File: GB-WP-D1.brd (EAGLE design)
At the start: 39.7 x 44.1 mm, 9 parts

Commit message: Add files via upload
WEMOS D1 mini size
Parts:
- removed JP2: (no value), pinhead_v2:1X05/OCT
- removed JP5: (no value), pinhead_v2:1X04/OCT
- added U$3: KAMENRIDER_LOGOV2_COLOR_OPAC, kamenrider:10_6_V2
- moved JP4 7.61 mm to (12.6, 27.7)
- moved U$2 7.61 mm to (12.6, 33.8)
- moved LED1 6.52 mm to (22.0, 32.5)
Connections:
- net 3.3V: no longer JP2.5, JP5.3
- net 5V: no longer JP2.4
- net D0: no longer JP2.1
- net D2: no longer JP5.1
- net D3: no longer JP2.2
- net GND: no longer JP2.3, JP5.4
- net N$7: no longer JP5.2
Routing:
- net 3.3V: track 114.3 -> 53.0 mm
- net D3: track 52.7 -> 0.00 mm, vias 1 -> 0
- net GND: track 90.4 -> 44.6 mm, vias 3 -> 1
- net 5V: track 43.4 -> 0.00 mm, vias 1 -> 0
- net D0: track 24.4 -> 0.00 mm
- net N$7: track 46.6 -> 25.7 mm
- net D2: track 41.0 -> 23.9 mm
- net D7: track 35.1 -> 27.5 mm
- net D6: track 35.1 -> 27.5 mm
- net D5: track 32.2 -> 24.6 mm
- net D4: track 26.7 -> 20.3 mm
- net N$5: track 33.4 -> 28.3 mm
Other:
- board size 39.7 x 44.1 mm -> 25.5 x 36.5 mm
- board text added: "4 WEMOS D1 mini"
- board text added: "https://git.io/JJk92 https://bit.ly/gbccd https://git.io/JJWkr"
- board text removed: "3V"
- board text removed: "https://bit.ly/gbccd"
- board text removed: "https://git.io/JJk92"

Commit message: Add files via upload
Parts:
- moved 4.7K 1.73 mm to (10.4, 9.61)
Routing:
- net N$5: track 28.3 -> 29.7 mm
- net D2: track 23.9 -> 25.3 mm
- net N$7: track 25.7 -> 27.0 mm
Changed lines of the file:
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@@
 <text x="13.081" y="2.413" size="0.8128" layer="21" font="vector" ratio="15" rot="R90">VCC</text>
 <text x="15.621" y="2.413" size="0.8128" layer="21" font="vector" ratio="15" rot="R90">GND</text>
-<text x="7.637584375" y="18.338246875" size="1.016" layer="22" ratio="12" rot="SMR270" align="center">https://git.io/JJk92
+<text x="7.192728125" y="17.109596875" size="0.762" layer="22" font="vector" ratio="12" distance="25" rot="SMR270" align="center">https://git.io/JJk92
 https://bit.ly/gbccd
 https://git.io/JJWkr</text>
@@
 </groups>
 <elements>
-<element name="4.7K" library="resistor" library_urn="urn:adsk.eagle:library:348" package="0207/10" package3d_urn="urn:adsk.eagle:package:23491/2" value="" x="9.652" y="11.176" smashed="yes" rot="SMR0">
-<attribute name="NAME" x="12.106859375" y="10.7617" size="1.016" layer="26" font="vector" ratio="15" rot="SMR0"/>
-<attribute name="VALUE" x="11.9126" y="10.541" size="1.27" layer="28" ratio="10" rot="SMR0"/>
+<element name="4.7K" library="resistor" library_urn="urn:adsk.eagle:library:348" package="0207/10" package3d_urn="urn:adsk.eagle:package:23491/2" value="" x="10.372240625" y="9.6084125" smashed="yes" rot="SMR0">
+<attribute name="NAME" x="12.8271" y="9.1941125" size="1.016" layer="26" font="vector" ratio="15" rot="SMR0"/>
+<attribute name="VALUE" x="12.632840625" y="8.9734125" size="1.27" layer="28" ratio="10" rot="SMR0"/>
 </element>
 <element name="U$2" library="link-port-pcb" package="GB-LINK-PCB" value="GB-LINK-PADS" x="12.594084375" y="33.7970875" smashed="yes"/>
@@
 <signal name="D2">
 <contactref element="JP1" pad="1"/>
-<wire x1="9.987215625" y1="2.878025" x2="8.593225" y2="2.878025" width="0.2032" layer="1"/>
+<wire x1="12.418403125" y1="2.878025" x2="8.593225" y2="2.878025" width="0.2032" layer="1"/>
 <wire x1="8.593225" y1="2.878025" x2="7.62" y2="1.9048" width="0.2032" layer="1"/>
 <wire x1="7.62" y1="1.27" x2="7.62" y2="1.9048" width="0.2032" layer="1"/>
-<wire x1="24.13" y1="16.997434375" x2="9.987215625" y2="2.878025" width="0.2032" layer="1"/>
+<wire x1="22.88016875" y1="13.322496875" x2="12.418403125" y2="2.878025" width="0.2032" layer="1"/>
 <contactref element="JP6" pad="4"/>
-<wire x1="24.13" y1="17.4752" x2="24.13" y2="16.997434375" width="0.2032" layer="1"/>
+<wire x1="24.13" y1="17.4752" x2="22.88016875" y2="16.22536875" width="0.2032" layer="1"/>
+<wire x1="22.88016875" y1="16.22536875" x2="22.88016875" y2="13.322496875" width="0.2032" layer="1"/>
 </signal>
 <signal name="D5">
@@
 <contactref element="4.7K" pad="2"/>
 <contactref element="JP3" pad="7"/>
-<wire x1="1.27" y1="9.8552" x2="3.2512" y2="9.8552" width="0.2032" layer="16"/>
-<wire x1="3.2512" y1="9.8552" x2="4.572" y2="11.176" width="0.2032" layer="16"/>
+<wire x1="1.27" y1="9.8552" x2="5.045453125" y2="9.8552" width="0.2032" layer="16"/>
+<wire x1="5.045453125" y1="9.8552" x2="5.292240625" y2="9.6084125" width="0.2032" layer="16"/>
 </signal>
 <signal name="D0">
@@
 <contactref element="4.7K" pad="1"/>
 <wire x1="16.404084375" y1="27.7010875" x2="18.152878125" y2="25.95229375" width="0.2032" layer="16"/>
-<wire x1="18.152878125" y1="12.690353125" x2="16.638525" y2="11.176" width="0.2032" layer="16"/>
-<wire x1="16.638525" y1="11.176" x2="14.732" y2="11.176" width="0.2032" layer="16"/>
-<wire x1="18.152878125" y1="25.95229375" x2="18.152878125" y2="12.690353125" width="0.2032" layer="16"/>
+<wire x1="18.152878125" y1="10.074178125" x2="17.6871125" y2="9.6084125" width="0.2032" layer="16"/>
+<wire x1="15.452240625" y1="9.6084125" x2="17.6871125" y2="9.6084125" width="0.2032" layer="16"/>
+<wire x1="18.152878125" y1="25.95229375" x2="18.152878125" y2="10.074178125" width="0.2032" layer="16"/>
 </signal>
 <signal name="N$7">
@@
 <wire x1="9.9061" y1="1.5239" x2="10.16" y2="1.27" width="0.2032" layer="16"/>
 <contactref element="JP6" pad="3"/>
-<wire x1="9.9061" y1="4.76236875" x2="11.2816875" y2="4.76236875" width="0.2032" layer="1"/>
-<wire x1="22.86" y1="16.34068125" x2="22.86" y2="18.923" width="0.2032" layer="1"/>
-<wire x1="22.86" y1="18.923" x2="23.9522" y2="20.0152" width="0.2032" layer="1"/>
+<wire x1="9.9061" y1="4.76236875" x2="13.569515625" y2="4.76236875" width="0.2032" layer="1"/>
+<wire x1="22.44691875" y1="13.639771875" x2="22.44691875" y2="18.50991875" width="0.2032" layer="1"/>
+<wire x1="22.44691875" y1="18.50991875" x2="23.9522" y2="20.0152" width="0.2032" layer="1"/>
 <wire x1="23.9522" y1="20.0152" x2="24.13" y2="20.0152" width="0.2032" layer="1"/>
-<wire x1="11.2816875" y1="4.76236875" x2="22.86" y2="16.34068125" width="0.2032" layer="1"/>
+<wire x1="13.569515625" y1="4.76236875" x2="22.44691875" y2="13.639771875" width="0.2032" layer="1"/>
 </signal>
 <signal name="A0">

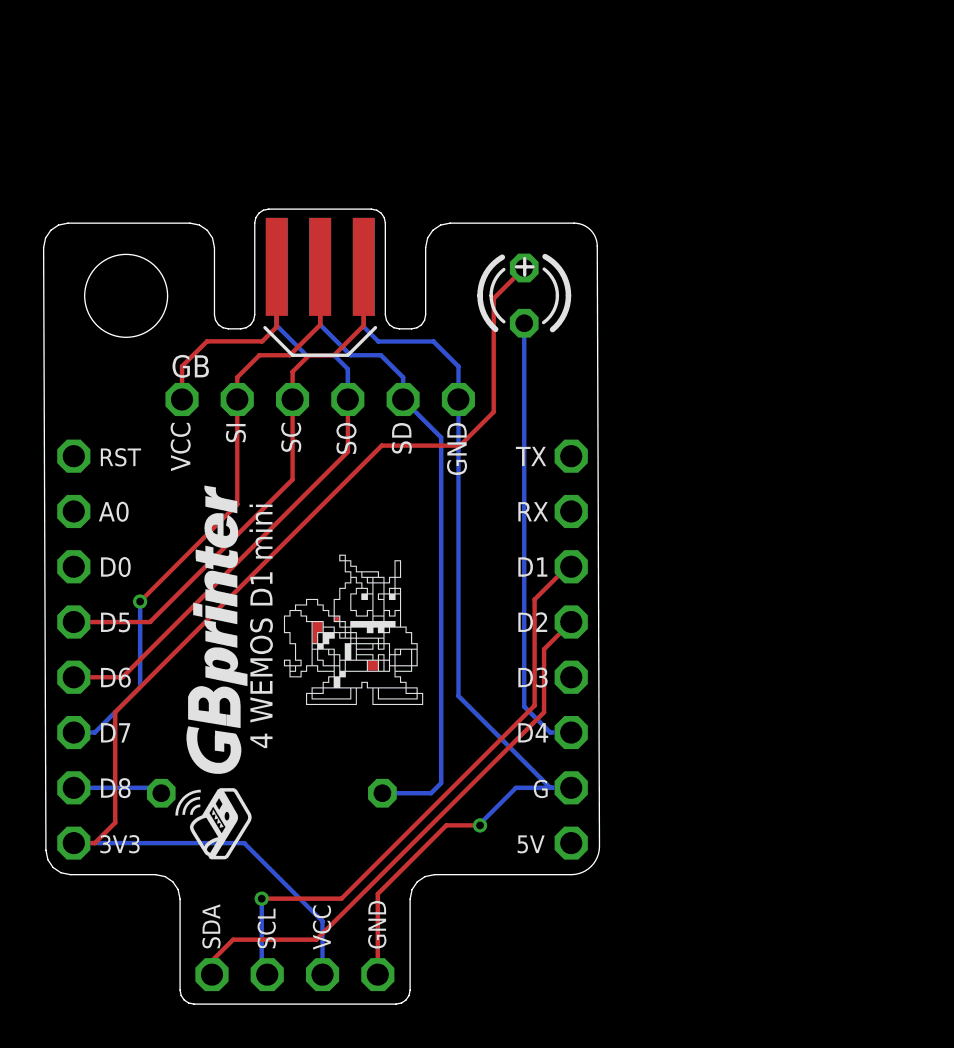
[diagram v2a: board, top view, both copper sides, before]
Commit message: Add files via upload
Added optional SMD 1206 fotprint for resistor and LED
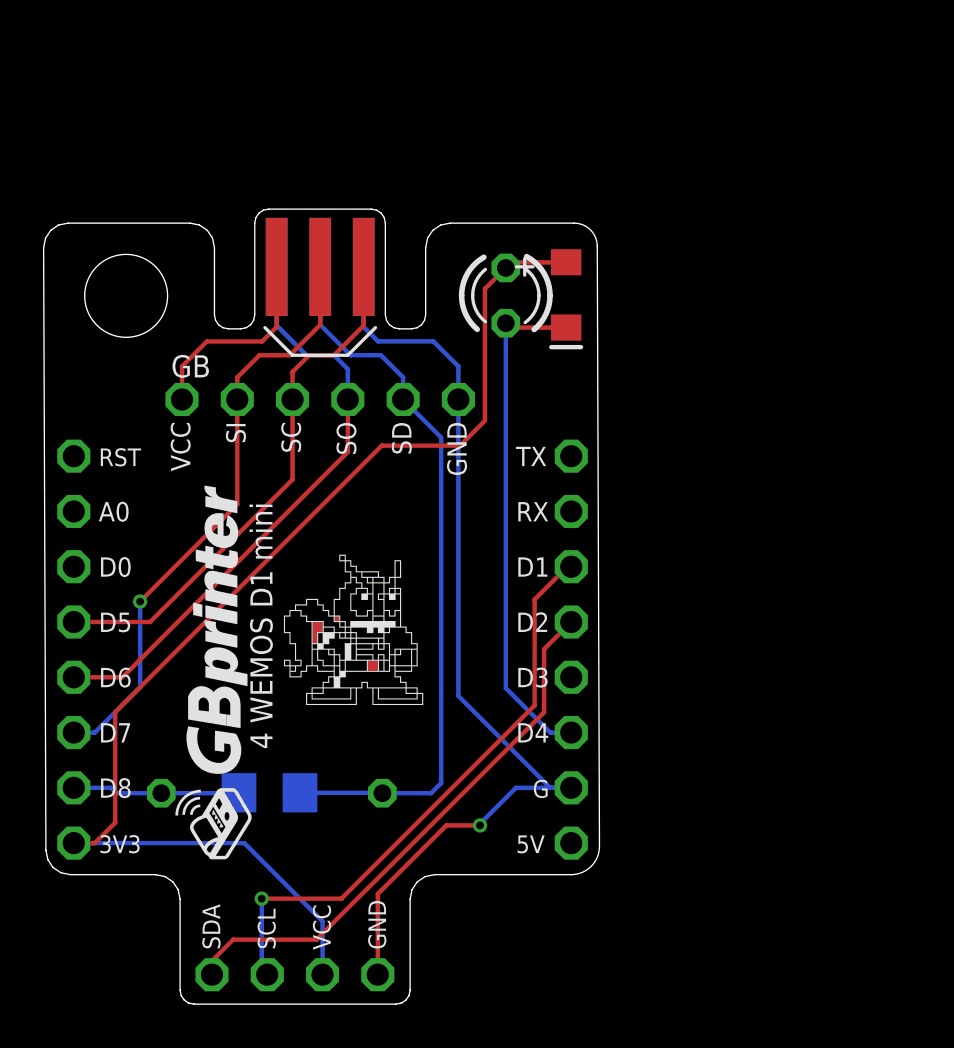
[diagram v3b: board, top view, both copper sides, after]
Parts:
- added D1: (no value), SparkFun-LED:LED-1206
- added R1: 4.7KOHM, SparkFun-Resistors:1206
- moved LED1 0.85 mm to (21.1, 32.5)
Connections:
- removed net D0: JP3.3
- removed net D3: JP6.5
- net 3.3V: now also D1.A
- net D4: now also D1.C
- net D8: now also R1.2
- net N$5: now also R1.1
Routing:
- net N$5: track 29.7 -> 33.7 mm
- net D8: track 4.12 -> 7.70 mm
- net D4: track 20.3 -> 23.5 mm
- net 3.3V: track 53.0 -> 55.6 mm
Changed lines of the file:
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@@
 <elements>
 <element name="4.7K" library="resistor" library_urn="urn:adsk.eagle:library:348" package="0207/10" package3d_urn="urn:adsk.eagle:package:23491/2" value="" x="10.372240625" y="9.6084125" smashed="yes" rot="SMR0">
-<attribute name="NAME" x="12.8271" y="9.1941125" size="1.016" layer="26" font="vector" ratio="15" rot="SMR0"/>
+<attribute name="NAME" x="13.6850375" y="10.973534375" size="1.016" layer="26" font="vector" ratio="15" rot="SMR0"/>
 <attribute name="VALUE" x="12.632840625" y="8.9734125" size="1.27" layer="28" ratio="10" rot="SMR0"/>
 </element>
@@
 <attribute name="VALUE" x="6.35" y="-1.905" size="1.27" layer="27"/>
 </element>
-<element name="LED1" library="led" library_urn="urn:adsk.eagle:library:259" package="LED3MM" package3d_urn="urn:adsk.eagle:package:15797/1" value="" x="21.970903125" y="32.475040625" smashed="yes" rot="R270">
-<attribute name="POPULARITY" value="97" x="21.970903125" y="32.475040625" size="1.778" layer="27" rot="R270" display="off"/>
-<attribute name="VALUE" x="20.319903125" y="30.570040625" size="1.27" layer="27" ratio="10" rot="R270"/>
+<element name="LED1" library="led" library_urn="urn:adsk.eagle:library:259" package="LED3MM" package3d_urn="urn:adsk.eagle:package:15797/1" value="" x="21.123559375" y="32.475040625" smashed="yes" rot="R270">
+<attribute name="POPULARITY" value="97" x="21.123559375" y="32.475040625" size="1.778" layer="27" rot="R270" display="off"/>
+<attribute name="VALUE" x="19.472559375" y="30.570040625" size="1.27" layer="27" ratio="10" rot="R270"/>
 </element>
 <element name="JP3" library="pinhead_v2" package="1X08/OCT" value="" x="1.27" y="16.2052" smashed="yes" rot="R270">
@@
 </element>
 <element name="U$3" library="kamenrider" package="10_6_V2" value="KAMENRIDER_LOGOV2_COLOR_OPAC" x="10.634165625" y="13.16560625" smashed="yes"/>
+<element name="D1" library="SparkFun-LED" package="LED-1206" value="" x="23.895103125" y="32.506234375" smashed="yes" rot="R270">
+<attribute name="VALUE" x="22.942603125" y="32.506234375" size="0.6096" layer="27" font="vector" ratio="20" rot="R270" align="top-center"/>
+</element>
+<element name="R1" library="SparkFun-Resistors" package="1206" value="4.7KOHM" x="10.26345625" y="9.62794375" smashed="yes" rot="MR0"/>
 </elements>
 <signals>
@@
 <contactref element="4.7K" pad="2"/>
 <contactref element="JP3" pad="7"/>
-<wire x1="1.27" y1="9.8552" x2="5.045453125" y2="9.8552" width="0.2032" layer="16"/>
-<wire x1="5.045453125" y1="9.8552" x2="5.292240625" y2="9.6084125" width="0.2032" layer="16"/>
-</signal>
-<signal name="D0">
-<contactref element="JP3" pad="3"/>
-</signal>
-<signal name="D3">
-<contactref element="JP6" pad="5"/>
+<wire x1="1.27" y1="9.8552" x2="2.980053125" y2="9.8552" width="0.2032" layer="16"/>
+<wire x1="3.226840625" y1="9.6084125" x2="5.292240625" y2="9.6084125" width="0.2032" layer="16"/>
+<wire x1="3.226840625" y1="9.6084125" x2="2.980053125" y2="9.8552" width="0.2032" layer="16"/>
+<contactref element="R1" pad="2"/>
+<wire x1="5.292240625" y1="9.6084125" x2="8.843925" y2="9.6084125" width="0.2032" layer="16"/>
+<wire x1="8.843925" y1="9.6084125" x2="8.86345625" y2="9.62794375" width="0.2032" layer="16"/>
 </signal>
 <signal name="D4">
 <contactref element="LED1" pad="K"/>
-<wire x1="21.970903125" y1="31.205040625" x2="21.970903125" y2="13.589096875" width="0.2032" layer="16"/>
-<wire x1="21.970903125" y1="13.589096875" x2="23.1648" y2="12.3952" width="0.2032" layer="16"/>
+<wire x1="21.123559375" y1="31.205040625" x2="21.123559375" y2="14.436440625" width="0.2032" layer="16"/>
+<wire x1="21.123559375" y1="14.436440625" x2="23.1648" y2="12.3952" width="0.2032" layer="16"/>
 <contactref element="JP6" pad="6"/>
 <wire x1="24.13" y1="12.3952" x2="23.1648" y2="12.3952" width="0.2032" layer="16"/>
+<contactref element="D1" pad="C"/>
+<wire x1="23.895103125" y1="31.006234375" x2="21.322365625" y2="31.006234375" width="0.2032" layer="1"/>
+<wire x1="21.322365625" y1="31.006234375" x2="21.123559375" y2="31.205040625" width="0.2032" layer="1"/>
 </signal>
 <signal name="5V">
@@
 <wire x1="12.7" y1="3.7187625" x2="9.1035625" y2="7.3152" width="0.2032" layer="16"/>
 <wire x1="12.7" y1="1.27" x2="12.7" y2="3.7187625" width="0.2032" layer="16"/>
-<wire x1="21.970903125" y1="33.745040625" x2="20.56600625" y2="32.34014375" width="0.2032" layer="1"/>
-<wire x1="20.56600625" y1="32.34014375" x2="20.56600625" y2="27.126725" width="0.2032" layer="1"/>
+<wire x1="21.123559375" y1="33.745040625" x2="20.16351875" y2="32.785" width="0.2032" layer="1"/>
+<wire x1="20.16351875" y1="32.785" x2="20.16351875" y2="26.7242375" width="0.2032" layer="1"/>
 <wire x1="3.175" y1="13.335" x2="15.42225" y2="25.58225" width="0.2032" layer="1"/>
 <wire x1="15.42225" y1="25.58225" x2="19.02153125" y2="25.58225" width="0.2032" layer="1"/>
-<wire x1="19.02153125" y1="25.58225" x2="20.56600625" y2="27.126725" width="0.2032" layer="1"/>
+<wire x1="19.02153125" y1="25.58225" x2="20.16351875" y2="26.7242375" width="0.2032" layer="1"/>
+<wire x1="21.3777625" y1="33.99924375" x2="21.123559375" y2="33.745040625" width="0.2032" layer="1"/>
+<contactref element="D1" pad="A"/>
+<wire x1="23.895103125" y1="34.006234375" x2="23.8881125" y2="33.99924375" width="0.2032" layer="1"/>
+<wire x1="23.8881125" y1="33.99924375" x2="21.3777625" y2="33.99924375" width="0.2032" layer="1"/>
 </signal>
 <signal name="N$1">
@@
 <wire x1="16.404084375" y1="27.7010875" x2="18.152878125" y2="25.95229375" width="0.2032" layer="16"/>
 <wire x1="18.152878125" y1="10.074178125" x2="17.6871125" y2="9.6084125" width="0.2032" layer="16"/>
-<wire x1="15.452240625" y1="9.6084125" x2="17.6871125" y2="9.6084125" width="0.2032" layer="16"/>
+<wire x1="15.452240625" y1="9.6084125" x2="15.5805375" y2="9.6084125" width="0.2032" layer="16"/>
+<wire x1="15.5805375" y1="9.6084125" x2="17.6871125" y2="9.6084125" width="0.2032" layer="16"/>
 <wire x1="18.152878125" y1="25.95229375" x2="18.152878125" y2="10.074178125" width="0.2032" layer="16"/>
+<wire x1="15.477275" y1="9.633446875" x2="15.452240625" y2="9.6084125" width="0.2032" layer="16"/>
+<contactref element="R1" pad="1"/>
+<wire x1="11.66345625" y1="9.62794375" x2="15.56100625" y2="9.62794375" width="0.2032" layer="16"/>
+<wire x1="15.56100625" y1="9.62794375" x2="15.5805375" y2="9.6084125" width="0.2032" layer="16"/>
 </signal>
 <signal name="N$7">
